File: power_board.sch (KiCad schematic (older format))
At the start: 39 parts, among them J1 RasPi_Conn2x20, J2 Power Supply, J3 MuddPi Conn, Q1 Q_NMOS_DGS, Q10 Q_NMOS_DGS, Q11 Q_NMOS_DGS, Q12 Q_NMOS_DGS, Q13 Q_PMOS_DGS, Q14 Q_PMOS_DGS, Q15 Q_PMOS_DGS, Q16 Q_PMOS_DGS, Q17 Q_NMOS_DGS, Q18 Q_NMOS_DGS, Q19 Q_NMOS_DGS, Q2 Q_NMOS_DGS, Q20 Q_NMOS_DGS, Q21 Q_PMOS_DGS, Q22 Q_PMOS_DGS, Q23 Q_PMOS_DGS, Q24 Q_PMOS_DGS, Q3 Q_NMOS_DGS, Q4 Q_NMOS_DGS, Q5 Q_PMOS_DGS, Q6 Q_PMOS_DGS, Q7 Q_PMOS_DGS, Q8 Q_PMOS_DGS, Q9 Q_NMOS_DGS

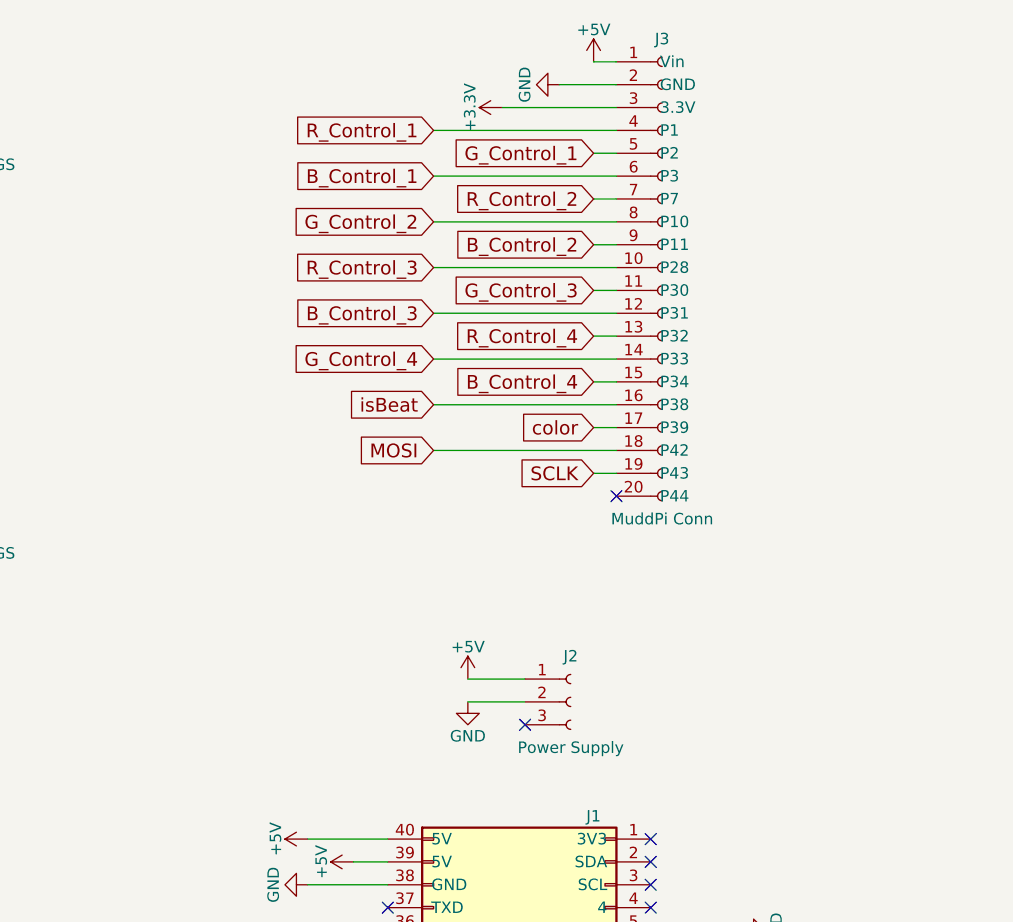
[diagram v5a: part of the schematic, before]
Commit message: Added schematic for the LED output connector
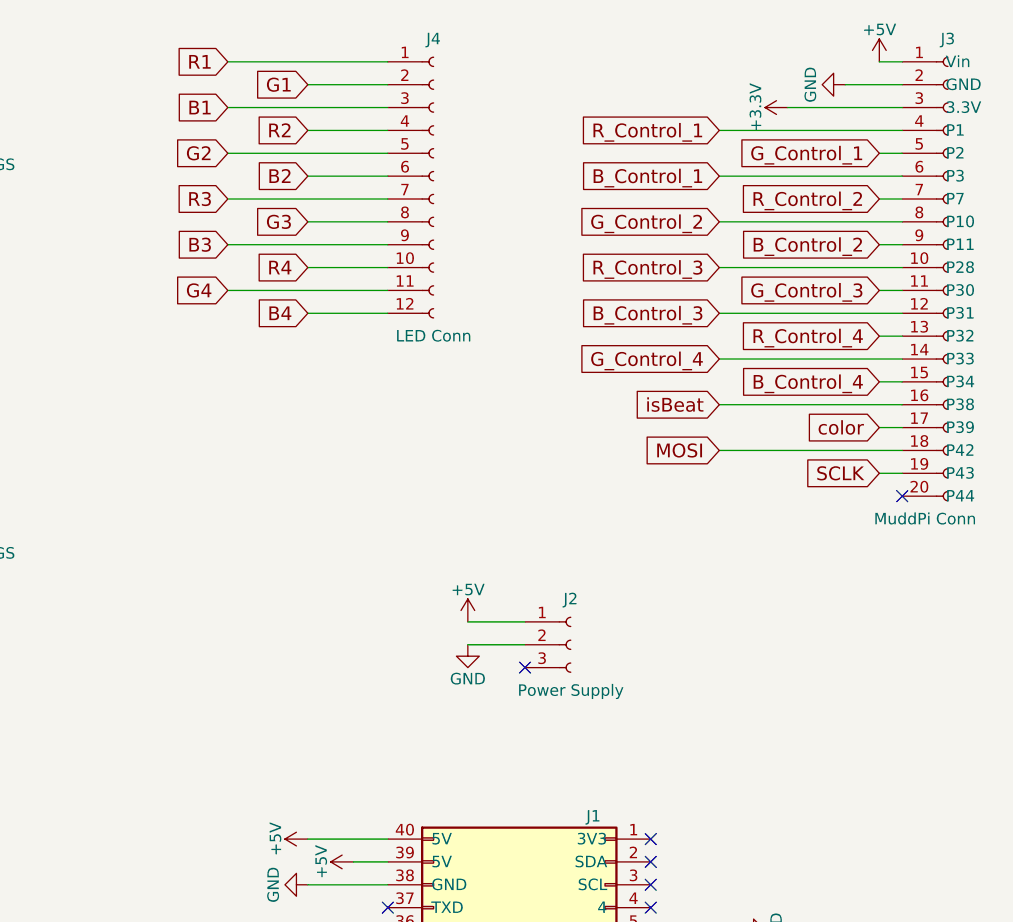
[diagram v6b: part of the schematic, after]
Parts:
- added J4: LED Conn, Connectors_Molex:Molex_KK-6410-12_12x2.54mm_Straight, symbol Conn_01x12_Female
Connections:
- net B1: now also J4.3 (Pin_3)
- net B2: now also J4.6 (Pin_6)
- net B3: now also J4.9 (Pin_9)
- net B4: now also J4.12 (Pin_12)
- net G1: now also J4.2 (Pin_2)
- net G2: now also J4.5 (Pin_5)
- net G3: now also J4.8 (Pin_8)
- net G4: now also J4.11 (Pin_11)
- net R1: now also J4.1 (Pin_1)
- net R2: now also J4.4 (Pin_4)
- net R3: now also J4.7 (Pin_7)
- net R4: now also J4.10 (Pin_10)
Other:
- moved on the sheet: J2, J3
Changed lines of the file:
@@
 L Conn_01x20_Female J3
 U 1 1 59DEA2F2
-P 9650 1700
-F 0 "J3" H 9650 2700 50  0000 C CNN
-F 1 "MuddPi Conn" H 9650 600 50  0000 C CNN
-F 2 "wall:Molex_1x20" H 9650 1700 50  0001 C CNN
-F 3 "" H 9650 1700 50  0001 C CNN
-F 4 "Sullins Connector Solutions" H 9650 1700 60  0001 C CNN "Manufacturer"
-F 5 "PPPC201LFBN-RC" H 9650 1700 60  0001 C CNN "Manufacturer PN"
-F 6 "0.100\" (2.54mm)" H 9650 1700 60  0001 C CNN "Pitch"
-	1    9650 1700
-	1    0    0    -1
-$EndComp
-$Comp
-L +5V #PWR48
+P 10900 1700
+F 0 "J3" H 10900 2700 50  0000 C CNN
+F 1 "MuddPi Conn" H 10800 600 50  0000 C CNN
+F 2 "wall:Molex_1x20" H 10900 1700 50  0001 C CNN
+F 3 "" H 10900 1700 50  0001 C CNN
+F 4 "Sullins Connector Solutions" H 10900 1700 60  0001 C CNN "Manufacturer"
+F 5 "PPPC201LFBN-RC" H 10900 1700 60  0001 C CNN "Manufacturer PN"
+F 6 "0.100\" (2.54mm)" H 10900 1700 60  0001 C CNN "Pitch"
+	1    10900 1700
+	1    0    0    -1
+$EndComp
+$Comp
+L +5V #PWR51
 U 1 1 59E0E942
-P 9350 800
-F 0 "#PWR48" H 9350 650 50  0001 C CNN
-F 1 "+5V" H 9350 940 50  0000 C CNN
-F 2 "" H 9350 800 50  0001 C CNN
-F 3 "" H 9350 800 50  0001 C CNN
-	1    9350 800
+P 10600 800
+F 0 "#PWR51" H 10600 650 50  0001 C CNN
+F 1 "+5V" H 10600 940 50  0000 C CNN
+F 2 "" H 10600 800 50  0001 C CNN
+F 3 "" H 10600 800 50  0001 C CNN
+	1    10600 800
 	1    0    0    -1
 $EndComp
@@
 	1650 1900 1650 2050
 Wire Wire Line
-	9350 800  9450 800
-$Comp
-L GND #PWR47
+	10600 800  10700 800
+$Comp
+L GND #PWR50
 U 1 1 59E0EB2B
-P 9200 900
-F 0 "#PWR47" H 9200 650 50  0001 C CNN
-F 1 "GND" H 9200 750 50  0000 C CNN
-F 2 "" H 9200 900 50  0001 C CNN
-F 3 "" H 9200 900 50  0001 C CNN
-	1    9200 900
+P 10450 900
+F 0 "#PWR50" H 10450 650 50  0001 C CNN
+F 1 "GND" H 10450 750 50  0000 C CNN
+F 2 "" H 10450 900 50  0001 C CNN
+F 3 "" H 10450 900 50  0001 C CNN
+	1    10450 900
 	0    1    1    0
 $EndComp
 Wire Wire Line
-	9200 900  9450 900
-$Comp
-L +3.3V #PWR46
+	10450 900  10700 900
+$Comp
+L +3.3V #PWR48
 U 1 1 59E0EC65
-P 8950 1000
-F 0 "#PWR46" H 8950 850 50  0001 C CNN
-F 1 "+3.3V" H 8950 1140 50  0000 C CNN
-F 2 "" H 8950 1000 50  0001 C CNN
-F 3 "" H 8950 1000 50  0001 C CNN
-	1    8950 1000
+P 10200 1000
+F 0 "#PWR48" H 10200 850 50  0001 C CNN
+F 1 "+3.3V" H 10200 1140 50  0000 C CNN
+F 2 "" H 10200 1000 50  0001 C CNN
+F 3 "" H 10200 1000 50  0001 C CNN
+	1    10200 1000
 	0    -1   -1   0
 $EndComp
 Wire Wire Line
-	8950 1000 9450 1000
-Text GLabel 8650 1100 0    60   Input ~ 0
+	10200 1000 10700 1000
+Text GLabel 9900 1100 0    60   Input ~ 0
 R_Control_1
-Text GLabel 9350 1200 0    60   Input ~ 0
+Text GLabel 10600 1200 0    60   Input ~ 0
 G_Control_1
-Text GLabel 8650 1300 0    60   Input ~ 0
+Text GLabel 9900 1300 0    60   Input ~ 0
 B_Control_1
-Text GLabel 9350 1400 0    60   Input ~ 0
+Text GLabel 10600 1400 0    60   Input ~ 0
 R_Control_2
-Text GLabel 8650 1500 0    60   Input ~ 0
+Text GLabel 9900 1500 0    60   Input ~ 0
 G_Control_2
-Text GLabel 9350 1600 0    60   Input ~ 0
+Text GLabel 10600 1600 0    60   Input ~ 0
 B_Control_2
-Text GLabel 8650 1700 0    60   Input ~ 0
+Text GLabel 9900 1700 0    60   Input ~ 0
 R_Control_3
-Text GLabel 9350 1800 0    60   Input ~ 0
+Text GLabel 10600 1800 0    60   Input ~ 0
 G_Control_3
-Text GLabel 8650 1900 0    60   Input ~ 0
+Text GLabel 9900 1900 0    60   Input ~ 0
 B_Control_3
-Text GLabel 9350 2000 0    60   Input ~ 0
+Text GLabel 10600 2000 0    60   Input ~ 0
 R_Control_4
-Text GLabel 8650 2100 0    60   Input ~ 0
+Text GLabel 9900 2100 0    60   Input ~ 0
 G_Control_4
-Text GLabel 9350 2200 0    60   Input ~ 0
+Text GLabel 10600 2200 0    60   Input ~ 0
 B_Control_4
-NoConn ~ 9450 2700
-Wire Wire Line
-	8650 1100 9450 1100
-Wire Wire Line
-	9350 1200 9450 1200
-Wire Wire Line
-	9450 1300 8650 1300
-Wire Wire Line
-	9350 1400 9450 1400
-Wire Wire Line
-	9450 1500 8650 1500
-Wire Wire Line
-	9350 1600 9450 1600
-Wire Wire Line
-	9450 1700 8650 1700
-Wire Wire Line
-	9350 1800 9450 1800
-Wire Wire Line
-	9450 1900 8650 1900
-Wire Wire Line
-	9350 2000 9450 2000
-Wire Wire Line
-	9450 2100 8650 2100
-Wire Wire Line
-	9350 2200 9450 2200
+NoConn ~ 10700 2700
+Wire Wire Line
+	9900 1100 10700 1100
+Wire Wire Line
+	10600 1200 10700 1200
+Wire Wire Line
+	10700 1300 9900 1300
+Wire Wire Line
+	10600 1400 10700 1400
+Wire Wire Line
+	10700 1500 9900 1500
+Wire Wire Line
+	10600 1600 10700 1600
+Wire Wire Line
+	10700 1700 9900 1700
+Wire Wire Line
+	10600 1800 10700 1800
+Wire Wire Line
+	10700 1900 9900 1900
+Wire Wire Line
+	10600 2000 10700 2000
+Wire Wire Line
+	10700 2100 9900 2100
+Wire Wire Line
+	10600 2200 10700 2200
 $Comp
 L +5V #PWR44
 U 1 1 59E11C95
-P 8800 3500
-F 0 "#PWR44" H 8800 3350 50  0001 C CNN
-F 1 "+5V" H 8800 3640 50  0000 C CNN
-F 2 "" H 8800 3500 50  0001 C CNN
-F 3 "" H 8800 3500 50  0001 C CNN
-	1    8800 3500
+P 8800 3250
+F 0 "#PWR44" H 8800 3100 50  0001 C CNN
+F 1 "+5V" H 8800 3390 50  0000 C CNN
+F 2 "" H 8800 3250 50  0001 C CNN
+F 3 "" H 8800 3250 50  0001 C CNN
+	1    8800 3250
 	1    0    0    -1
 $EndComp
@@
 L GND #PWR45
 U 1 1 59E11D45
-P 8800 3600
-F 0 "#PWR45" H 8800 3350 50  0001 C CNN
-F 1 "GND" H 8800 3450 50  0000 C CNN
-F 2 "" H 8800 3600 50  0001 C CNN
-F 3 "" H 8800 3600 50  0001 C CNN
-	1    8800 3600
-	1    0    0    -1
-$EndComp
-Wire Wire Line
-	8800 3500 9050 3500
-Wire Wire Line
-	8800 3600 9050 3600
+P 8800 3350
+F 0 "#PWR45" H 8800 3100 50  0001 C CNN
+F 1 "GND" H 8800 3200 50  0000 C CNN
+F 2 "" H 8800 3350 50  0001 C CNN
+F 3 "" H 8800 3350 50  0001 C CNN
+	1    8800 3350
+	1    0    0    -1
+$EndComp
+Wire Wire Line
+	8800 3250 9050 3250
+Wire Wire Line
+	8800 3350 9050 3350
 $Comp
 L +5V #PWR38
@@
 Wire Wire Line
 	8100 5200 8450 5200
-Text GLabel 8650 2300 0    60   Input ~ 0
+Text GLabel 9900 2300 0    60   Input ~ 0
 isBeat
 Wire Wire Line
-	9450 2300 8650 2300
+	10700 2300 9900 2300
 Text GLabel 9950 5700 2    60   Input ~ 0
 color
 Wire Wire Line
 	9950 5700 9600 5700
-Text GLabel 9350 2400 0    60   Input ~ 0
+Text GLabel 10600 2400 0    60   Input ~ 0
 color
 Wire Wire Line
-	9350 2400 9450 2400
-Text GLabel 8650 2500 0    60   Input ~ 0
+	10600 2400 10700 2400
+Text GLabel 9900 2500 0    60   Input ~ 0
 MOSI
-Text GLabel 9350 2600 0    60   Input ~ 0
+Text GLabel 10600 2600 0    60   Input ~ 0
 SCLK
 Text GLabel 9950 5100 2    60   Input ~ 0
@@
 	9600 5100 9950 5100
 Wire Wire Line
-	8650 2500 9450 2500
-Wire Wire Line
-	9350 2600 9450 2600
+	9900 2500 10700 2500
+Wire Wire Line
+	10600 2600 10700 2600
 NoConn ~ 9600 4200
 NoConn ~ 9600 4300
@@
 NoConn ~ 9600 5800
 $Comp
-L GND #PWR49
+L GND #PWR46
 U 1 1 59E58CA5
 P 10000 4600
-F 0 "#PWR49" H 10000 4350 50  0001 C CNN
+F 0 "#PWR46" H 10000 4350 50  0001 C CNN
 F 1 "GND" H 10000 4450 50  0000 C CNN
 F 2 "" H 10000 4600 50  0001 C CNN
@@
 $EndComp
 $Comp
-L GND #PWR51
+L GND #PWR49
 U 1 1 59E58D55
 P 10250 5400
-F 0 "#PWR51" H 10250 5150 50  0001 C CNN
+F 0 "#PWR49" H 10250 5150 50  0001 C CNN
 F 1 "GND" H 10250 5250 50  0000 C CNN
 F 2 "" H 10250 5400 50  0001 C CNN
@@
 $EndComp
 $Comp
-L GND #PWR50
+L GND #PWR47
 U 1 1 59E58E05
 P 10000 6100
-F 0 "#PWR50" H 10000 5850 50  0001 C CNN
+F 0 "#PWR47" H 10000 5850 50  0001 C CNN
 F 1 "GND" H 10000 5950 50  0000 C CNN
 F 2 "" H 10000 6100 50  0001 C CNN
@@
 L Conn_01x03_Female J2
 U 1 1 59E6A3FD
-P 9250 3600
-F 0 "J2" H 9250 3800 50  0000 C CNN
-F 1 "Power Supply" H 9250 3400 50  0000 C CNN
-F 2 "Connect:BARREL_JACK" H 9250 3600 50  0001 C CNN
-F 3 "" H 9250 3600 50  0001 C CNN
-	1    9250 3600
-	1    0    0    -1
-$EndComp
-NoConn ~ 9050 3700
+P 9250 3350
+F 0 "J2" H 9250 3550 50  0000 C CNN
+F 1 "Power Supply" H 9250 3150 50  0000 C CNN
+F 2 "Connect:BARREL_JACK" H 9250 3350 50  0001 C CNN
+F 3 "" H 9250 3350 50  0001 C CNN
+	1    9250 3350
+	1    0    0    -1
+$EndComp
+NoConn ~ 9050 3450
 $Comp
 L Q_NMOS_DGS Q2
@@
 Wire Wire Line
 	9600 5400 10250 5400
+$Comp
+L Conn_01x12_Female J4
+U 1 1 59E81833
+P 8650 1300
+F 0 "J4" H 8650 1900 50  0000 C CNN
+F 1 "LED Conn" H 8650 600 50  0000 C CNN
+F 2 "Connectors_Molex:Molex_KK-6410-12_12x2.54mm_Straight" H 8650 1300 50  0001 C CNN
+F 3 "" H 8650 1300 50  0001 C CNN
+	1    8650 1300
+	1    0    0    -1
+$EndComp
+Text GLabel 7750 800  0    60   Input ~ 0
+R1
+Wire Wire Line
+	7750 800  8450 800
+Text GLabel 8100 900  0    60   Input ~ 0
+G1
+Text GLabel 7750 1000 0    60   Input ~ 0
+B1
+Text GLabel 8100 1100 0    60   Input ~ 0
+R2
+Text GLabel 7750 1200 0    60   Input ~ 0
+G2
+Text GLabel 8100 1300 0    60   Input ~ 0
+B2
+Text GLabel 7750 1400 0    60   Input ~ 0
+R3
+Text GLabel 8100 1500 0    60   Input ~ 0
+G3
+Text GLabel 7750 1600 0    60   Input ~ 0
+B3
+Text GLabel 8100 1700 0    60   Input ~ 0
+R4
+Text GLabel 7750 1800 0    60   Input ~ 0
+G4
+Text GLabel 8100 1900 0    60   Input ~ 0
+B4
+Wire Wire Line
+	8100 900  8450 900
+Wire Wire Line
+	7750 1000 8450 1000
+Wire Wire Line
+	8100 1100 8450 1100
+Wire Wire Line
+	7750 1200 8450 1200
+Wire Wire Line
+	8100 1300 8450 1300
+Wire Wire Line
+	7750 1400 8450 1400
+Wire Wire Line
+	8100 1500 8450 1500
+Wire Wire Line
+	7750 1600 8450 1600
+Wire Wire Line
+	8100 1700 8450 1700
+Wire Wire Line
+	7750 1800 8450 1800
+Wire Wire Line
+	8100 1900 8450 1900
 $EndSCHEMATC
